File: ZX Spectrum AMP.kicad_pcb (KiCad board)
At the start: 2 copper layers, 55 x 48 mm, 13 parts, among them IC1 LM386, J1 9V DC(in), J2 Input (MIC), J3 9V DC(out), P1 4,7K Ohm

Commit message: updated
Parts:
- added G***: LOGO, LOGO, F.Cu at (59.5, 59.9)
- added H1: MountingHole, MountingHole:MountingHole_3.5mm, F.Cu at (34.5, 44.8)
- added H2: MountingHole, MountingHole:MountingHole_3.5mm, F.Cu at (84.5, 44.8)
- added H3: MountingHole, MountingHole:MountingHole_3.5mm, F.Cu at (34.5, 75.1)
- added H4: MountingHole, MountingHole:MountingHole_3.5mm, F.Cu at (84.5, 75.1)
- added P2: 50K, Potentiometer_THT:Potentiometer_Piher_PT-10-V10_Vertical, F.Cu at (41.7, 72.0)
- added REF**: KiCad-Logo2_5mm_SilkScreen, Symbol:KiCad-Logo2_5mm_SilkScreen, F.Cu at (48.4, 59.0)
- P1: value 4,7K Ohm -> 4.7K
- R1: value 10 Ohm -> 10
- moved J3 36.8 mm to (60.0, 45.4), turned to 90 degrees
- moved MIC1 27.9 mm to (49.8, 45.4), turned to 90 degrees
- moved HT1 8.14 mm to (44.8, 36.7), turned to -90 degrees
- moved P1 7.63 mm to (38.8, 54.7)
- moved J2 6.76 mm to (57.9, 69.2)
- moved C1 4.57 mm to (62.5, 56.9)
- moved C2 4.56 mm to (85.9, 56.9)
- moved C3 4.56 mm to (85.9, 63.4)
- moved C5 3.79 mm to (68.0, 46.3)
- moved IC1 3.62 mm to (70.0, 57.0)
- moved R1 3.35 mm to (73.0, 51.3)
- moved J1 1.77 mm to (73.8, 71.2)
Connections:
- J2 pad 1: Net-(MIC1-Pin_1) -> Net-(J2-Pad1)
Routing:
- net Net-(J2-Pad1): track 0.00 -> 19.8 mm
- net GND: track 130.7 -> 148.9 mm
- net +9V: track 33.6 -> 50.8 mm
- net Net-(IC1-+): track 33.6 -> 42.6 mm
- net Net-(MIC1-Pin_1): track 38.1 -> 43.4 mm
- net Net-(C4-Pad2): track 27.5 -> 32.5 mm
- net Net-(IC1-BYPASS): track 8.07 -> 9.39 mm
- net Net-(C5-Pad2): track 4.77 -> 6.03 mm
- net Net-(C4-Pad1): track 33.2 -> 32.2 mm
- added copper zone on B.Cu, net GND
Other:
- board size 55 x 48 mm -> 63.2 x 50.3 mm

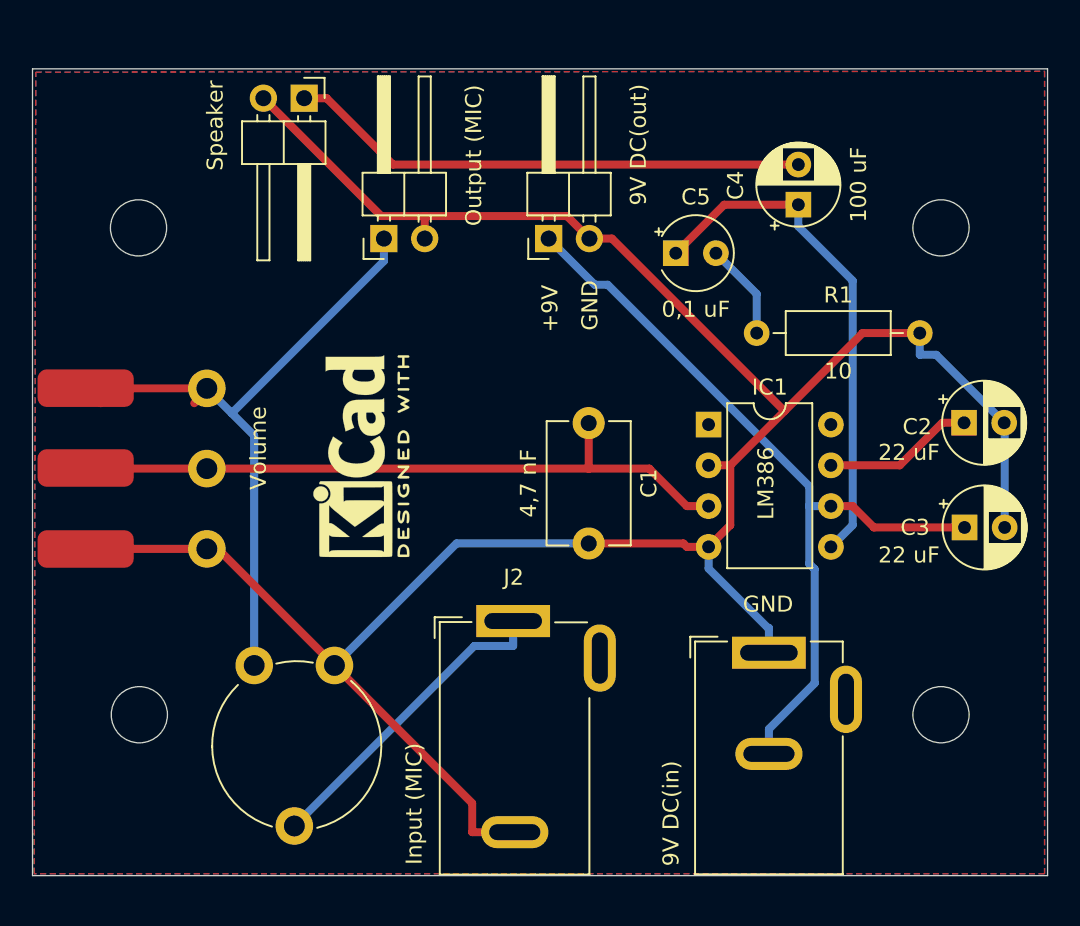
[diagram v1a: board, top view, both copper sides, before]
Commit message: v0.3 - add logo + corrected text
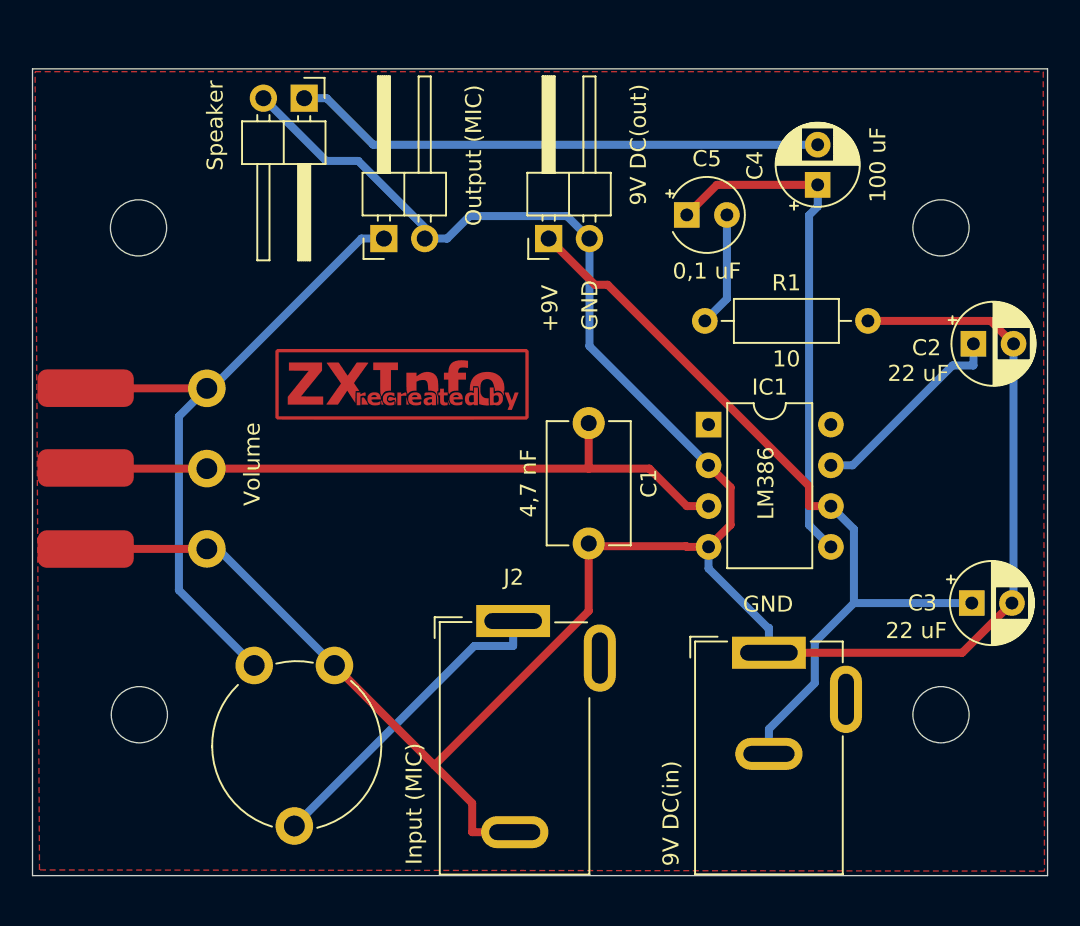
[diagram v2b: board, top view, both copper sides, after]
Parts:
- removed REF**: KiCad-Logo2_5mm_SilkScreen, Symbol:KiCad-Logo2_5mm_SilkScreen
- added G200: LOGO, ZXAmp:ZXInfo_kicad_logo_copper_16.5x5, F.Cu at (50.9, 54.5)
- moved C2 4.96 mm to (86.5, 52.0)
- moved C3 4.73 mm to (86.4, 68.1)
- moved R1 3.32 mm to (69.8, 50.5)
- moved C5 2.48 mm to (68.6, 44.0)
- moved C4 1.73 mm to (76.8, 42.1)
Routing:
- net GND: track 148.9 -> 160.1 mm
- net Net-(IC1-BYPASS): track 9.39 -> 12.8 mm
- net Net-(C5-Pad2): track 6.03 -> 7.17 mm
- net Net-(MIC1-Pin_1): track 43.4 -> 42.4 mm
- net Net-(C4-Pad2): track 32.5 -> 33.2 mm
- removed copper zone on B.Cu, net GND
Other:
- board text added: "Spectrum forstærker v0.3 (NE - 84)"
- board text removed: "Spectrum forstæker v0.2 (NE - 84)"
